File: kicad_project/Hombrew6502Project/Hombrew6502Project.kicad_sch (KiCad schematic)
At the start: 75 parts, among them J101 Clock input, J102 Conn_01x02_Pin, J103 Conn_01x02_Pin, U101 74HC04, U102 74HC74, U103 74HC74, U104 W65C02SxPL, U105 CD74HC4002M96, U106 SN74LS07, U107 74AHC2G00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

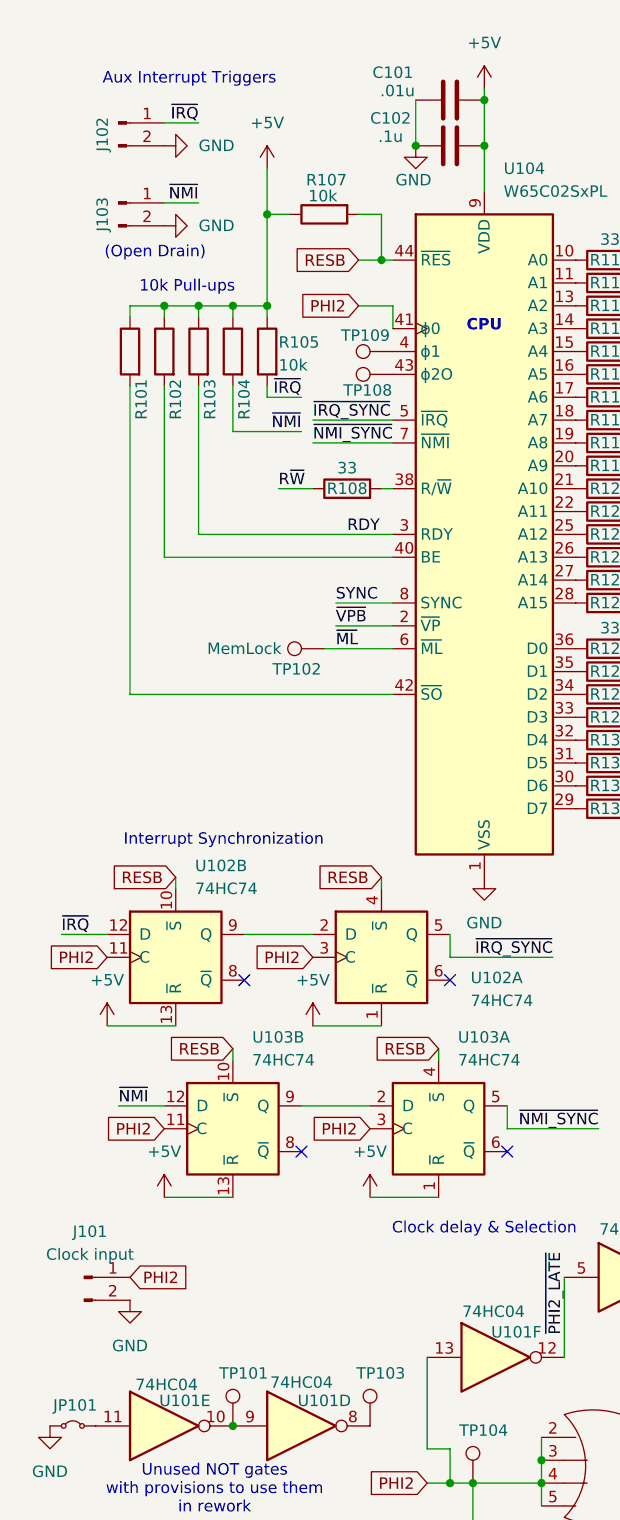
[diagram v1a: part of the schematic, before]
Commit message: footprint assignments and separate project for RAM board
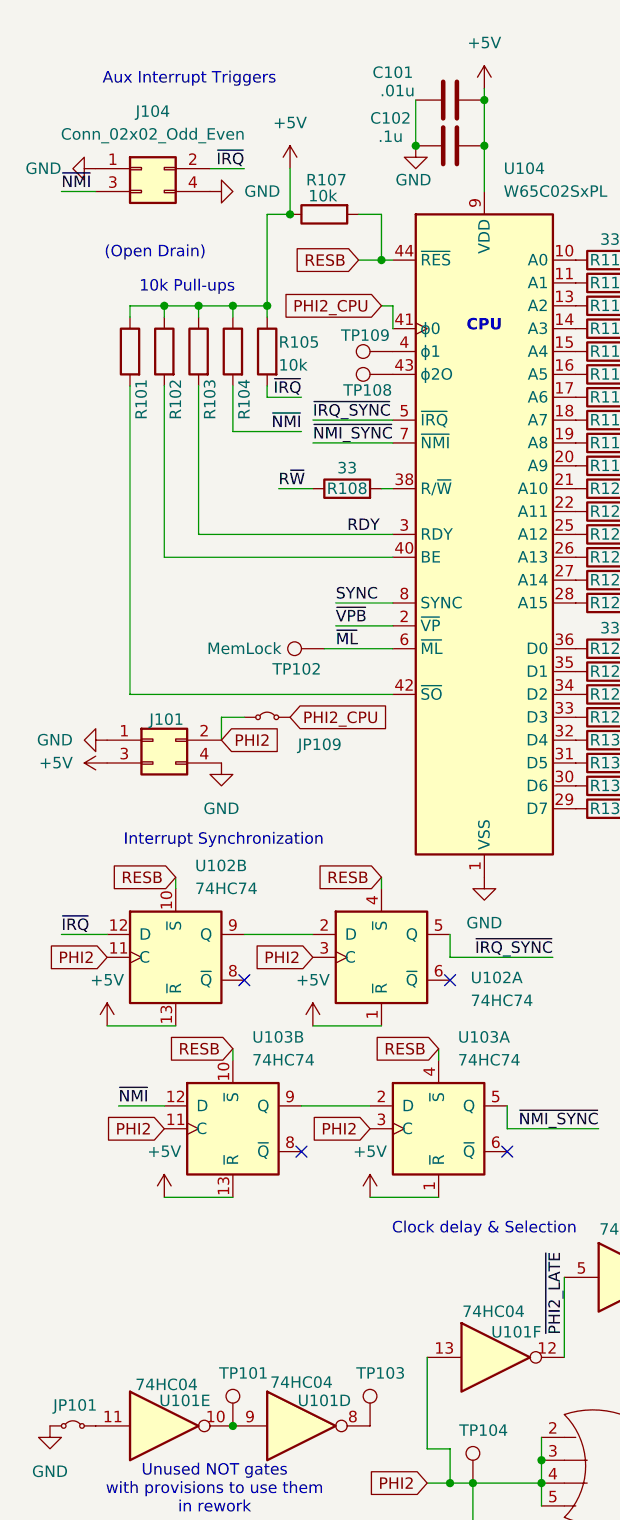
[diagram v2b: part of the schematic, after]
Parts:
- removed J101: Clock input, symbol Connector:Conn_01x02_Pin
- removed J102, J103: Conn_01x02_Pin, symbol Connector:Conn_01x02_Pin
- added J101, J104: Conn_02x02_Odd_Even, Connector_PinHeader_2.54mm:PinHeader_2x02_P2.54mm_Vertical_SMD, symbol Connector_Generic:Conn_02x02_Odd_Even
- added JP109: Jumper_2_Small_Bridged, Jumper:SolderJumper-2_P1.3mm_Bridged2Bar_Pad1.0x1.5mm, symbol Jumper:Jumper_2_Small_Bridged
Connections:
- net +5V: now also J101.3 (Pin_3)
- net GND: now also J101.1 (Pin_1), J101.4 (Pin_4), J104.1 (Pin_1), J104.4 (Pin_4)
- net PHI2: now also J101.2 (Pin_2), JP109.1 (A); no longer U104.41 (ϕ0)
- net ~{IRQ}: now also J104.2 (Pin_2)
- net ~{NMI}: now also J104.3 (Pin_3)
- new net PHI2_CPU: JP109.2 (B), U104.41 (ϕ0)

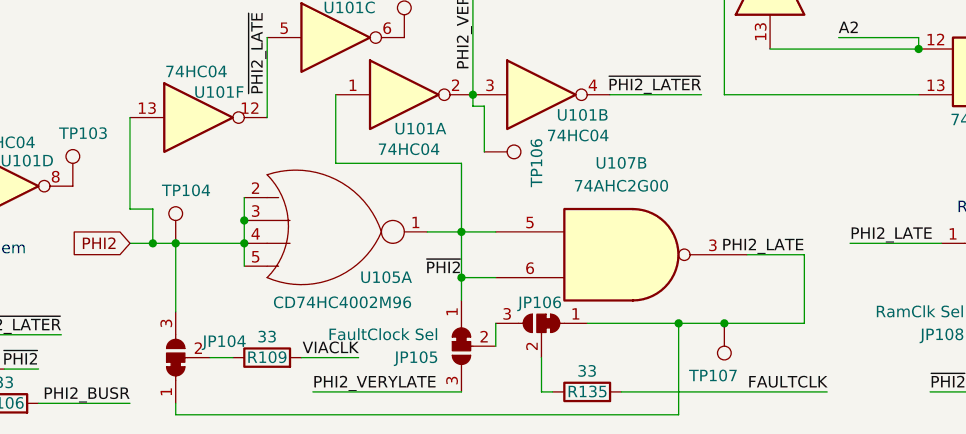
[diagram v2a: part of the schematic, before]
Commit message: Peripheral io layout done; snapshot of current state before redoing much of the rest of the layout.
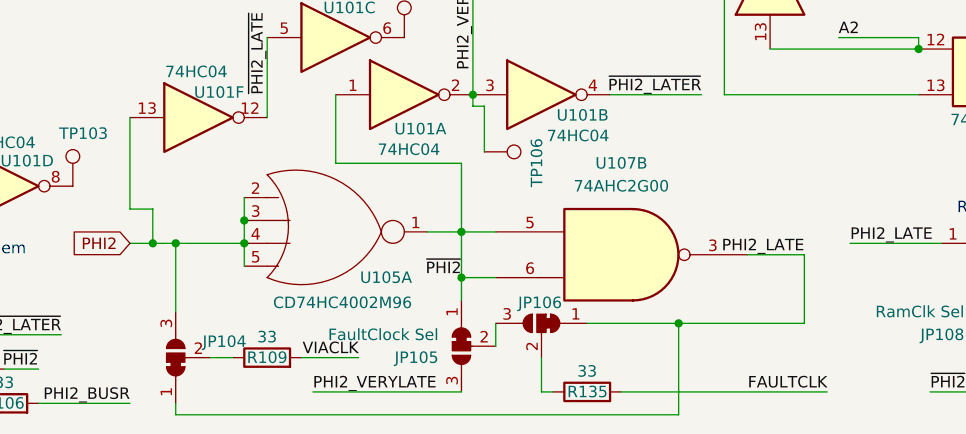
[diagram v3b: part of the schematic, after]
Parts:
- removed TP104, TP107: TestPoint, TestPoint:TestPoint_Pad_D1.5mm, symbol Connector:TestPoint
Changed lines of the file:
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@@
 	)
 	(junction
-		(at 124.46 185.42)
-		(diameter 0)
-		(color 0 0 0 0)
-	)
-	(junction
 		(at 102.87 43.18)
 		(diameter 0)
@@
 	(wire
 		(pts
-			(xy 124.46 185.42) (xy 133.35 185.42)
-		)
-		(stroke
-			(width 0)
-			(type default)
-		)
-	)
-	(wire
-		(pts
 			(xy 33.02 45.72) (xy 36.83 45.72)
 		)
@@
 	(wire
 		(pts
-			(xy 124.46 185.42) (xy 119.38 185.42)
+			(xy 119.38 185.42) (xy 133.35 185.42)
 		)
 		(stroke
@@
 	)
 	(symbol
-		(lib_id "Connector:TestPoint")
-		(at 63.5 176.53 0)
-		(unit 1)
-		(exclude_from_sim no)
-		(in_bom yes)
-		(on_board yes)
-		(dnp no)
-		(property "Reference" "TP104"
-			(at 61.976 170.688 0)
-			(effects
-				(font
-					(size 1.27 1.27)
-				)
-				(justify left)
-			)
-		)
-		(property "Value" "TestPoint"
-			(at 66.04 174.4979 0)
-			(effects
-				(font
-					(size 1.27 1.27)
-				)
-				(justify left)
-				(hide yes)
-			)
-		)
-		(property "Footprint" "TestPoint:TestPoint_Pad_D1.5mm"
-			(at 68.58 176.53 0)
-			(effects
-				(font
-					(size 1.27 1.27)
-				)
-				(hide yes)
-			)
-		)
-		(property "Datasheet" "~"
-			(at 68.58 176.53 0)
-			(effects
-				(font
-					(size 1.27 1.27)
-				)
-				(hide yes)
-			)
-		)
-		(property "Description" "test point"
-			(at 63.5 176.53 0)
-			(effects
-				(font
-					(size 1.27 1.27)
-				)
-				(hide yes)
-			)
-		)
-		(property "t_pd (ns)" ""
-			(at 63.5 176.53 0)
-			(effects
-				(font
-					(size 1.27 1.27)
-				)
-				(hide yes)
-			)
-		)
-		(pin "1"
-		)
-		(instances
-			(project "6502sbc"
-				(path "/dc8636f6-e59e-4c75-ae27-408ad57a23de"
-					(reference "TP104")
-					(unit 1)
-				)
-			)
-		)
-	)
-	(symbol
 		(lib_id "Device:R")
 		(at 78.74 99.06 90)
@@
 					(unit 1)
 				)
-			)
-		)
-	)
-	(symbol
-		(lib_id "Connector:TestPoint")
-		(at 124.46 185.42 180)
-		(unit 1)
-		(exclude_from_sim no)
-		(in_bom yes)
-		(on_board yes)
-		(dnp no)
-		(property "Reference" "TP107"
-			(at 125.984 191.262 0)
-			(effects
-				(font
-					(size 1.27 1.27)
-				)
-				(justify left)
-			)
-		)
-		(property "Value" "TestPoint"
-			(at 121.92 187.4521 0)
-			(effects
-				(font
-					(size 1.27 1.27)
-				)
-				(justify left)
-				(hide yes)
-			)
-		)
-		(property "Footprint" "TestPoint:TestPoint_Pad_D1.5mm"
-			(at 119.38 185.42 0)
-			(effects
-				(font
-					(size 1.27 1.27)
-				)
-				(hide yes)
-			)
-		)
-		(property "Datasheet" "~"
-			(at 119.38 185.42 0)
-			(effects
-				(font
-					(size 1.27 1.27)
-				)
-				(hide yes)
-			)
-		)
-		(property "Description" "test point"
-			(at 124.46 185.42 0)
-			(effects
-				(font
-					(size 1.27 1.27)
-				)
-				(hide yes)
-			)
-		)
-		(property "t_pd (ns)" ""
-			(at 124.46 185.42 0)
-			(effects
-				(font
-					(size 1.27 1.27)
-				)
-				(hide yes)
-			)
-		)
-		(pin "1"
-		)
-		(instances
-			(project "6502sbc"
-				(path "/dc8636f6-e59e-4c75-ae27-408ad57a23de"
-					(reference "TP107")
-					(unit 1)
-				)

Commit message: Layout mostly finished
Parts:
- removed TP103: TestPoint, TestPoint:TestPoint_Pad_D2.5mm, symbol Connector:TestPoint
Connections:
- no-connect marks 6 -> 7
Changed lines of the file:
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@@
 	(title_block
 		(title "65c02 Homebrew")
-		(rev "Prelim")
+		(rev "Rev A")
 		(company "Joseph R. Freeston")
 		(comment 2 "https://github.com/snorklerjoe/useful6502")
@@
 	)
 	(no_connect
+		(at 52.07 170.18)
+	)
+	(no_connect
 		(at 128.27 101.6)
 	)
@@
 					(unit 1)
 				)
-			)
-		)
-	)
-	(symbol
-		(lib_id "Connector:TestPoint")
-		(at 52.07 170.18 0)
-		(unit 1)
-		(exclude_from_sim no)
-		(in_bom yes)
-		(on_board yes)
-		(dnp no)
-		(property "Reference" "TP103"
-			(at 50.546 164.338 0)
-			(effects
-				(font
-					(size 1.27 1.27)
-				)
-				(justify left)
-			)
-		)
-		(property "Value" "TestPoint"
-			(at 54.61 168.1479 0)
-			(effects
-				(font
-					(size 1.27 1.27)
-				)
-				(justify left)
-				(hide yes)
-			)
-		)
-		(property "Footprint" "TestPoint:TestPoint_Pad_D2.5mm"
-			(at 57.15 170.18 0)
-			(effects
-				(font
-					(size 1.27 1.27)
-				)
-				(hide yes)
-			)
-		)
-		(property "Datasheet" "~"
-			(at 57.15 170.18 0)
-			(effects
-				(font
-					(size 1.27 1.27)
-				)
-				(hide yes)
-			)
-		)
-		(property "Description" "test point"
-			(at 52.07 170.18 0)
-			(effects
-				(font
-					(size 1.27 1.27)
-				)
-				(hide yes)
-			)
-		)
-		(property "t_pd (ns)" ""
-			(at 52.07 170.18 0)
-			(effects
-				(font
-					(size 1.27 1.27)
-				)
-				(hide yes)
-			)
-		)
-		(pin "1"
-		)
-		(instances
-			(project "6502sbc"
-				(path "/dc8636f6-e59e-4c75-ae27-408ad57a23de"
-					(reference "TP103")
-					(unit 1)
-				)
